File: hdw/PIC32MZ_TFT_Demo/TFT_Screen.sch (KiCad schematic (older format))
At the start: 2 parts

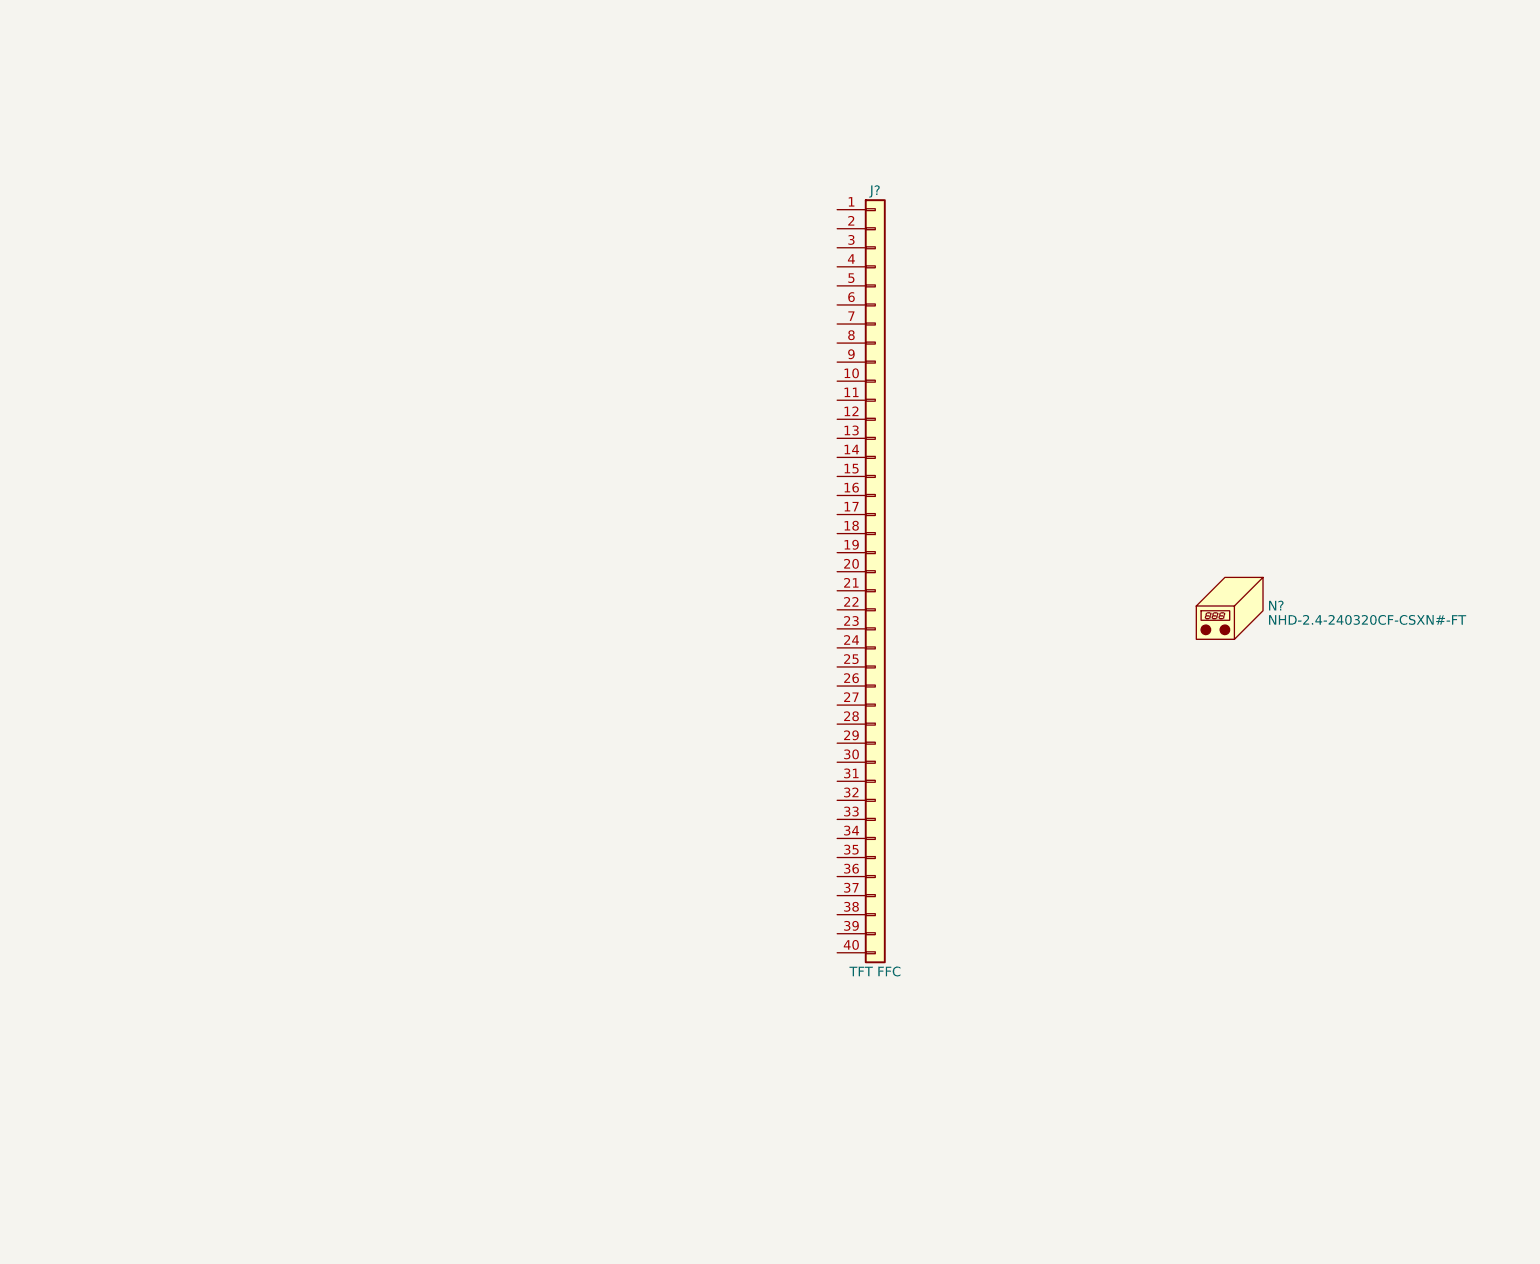
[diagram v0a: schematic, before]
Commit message: Added TFT screen sch sheet
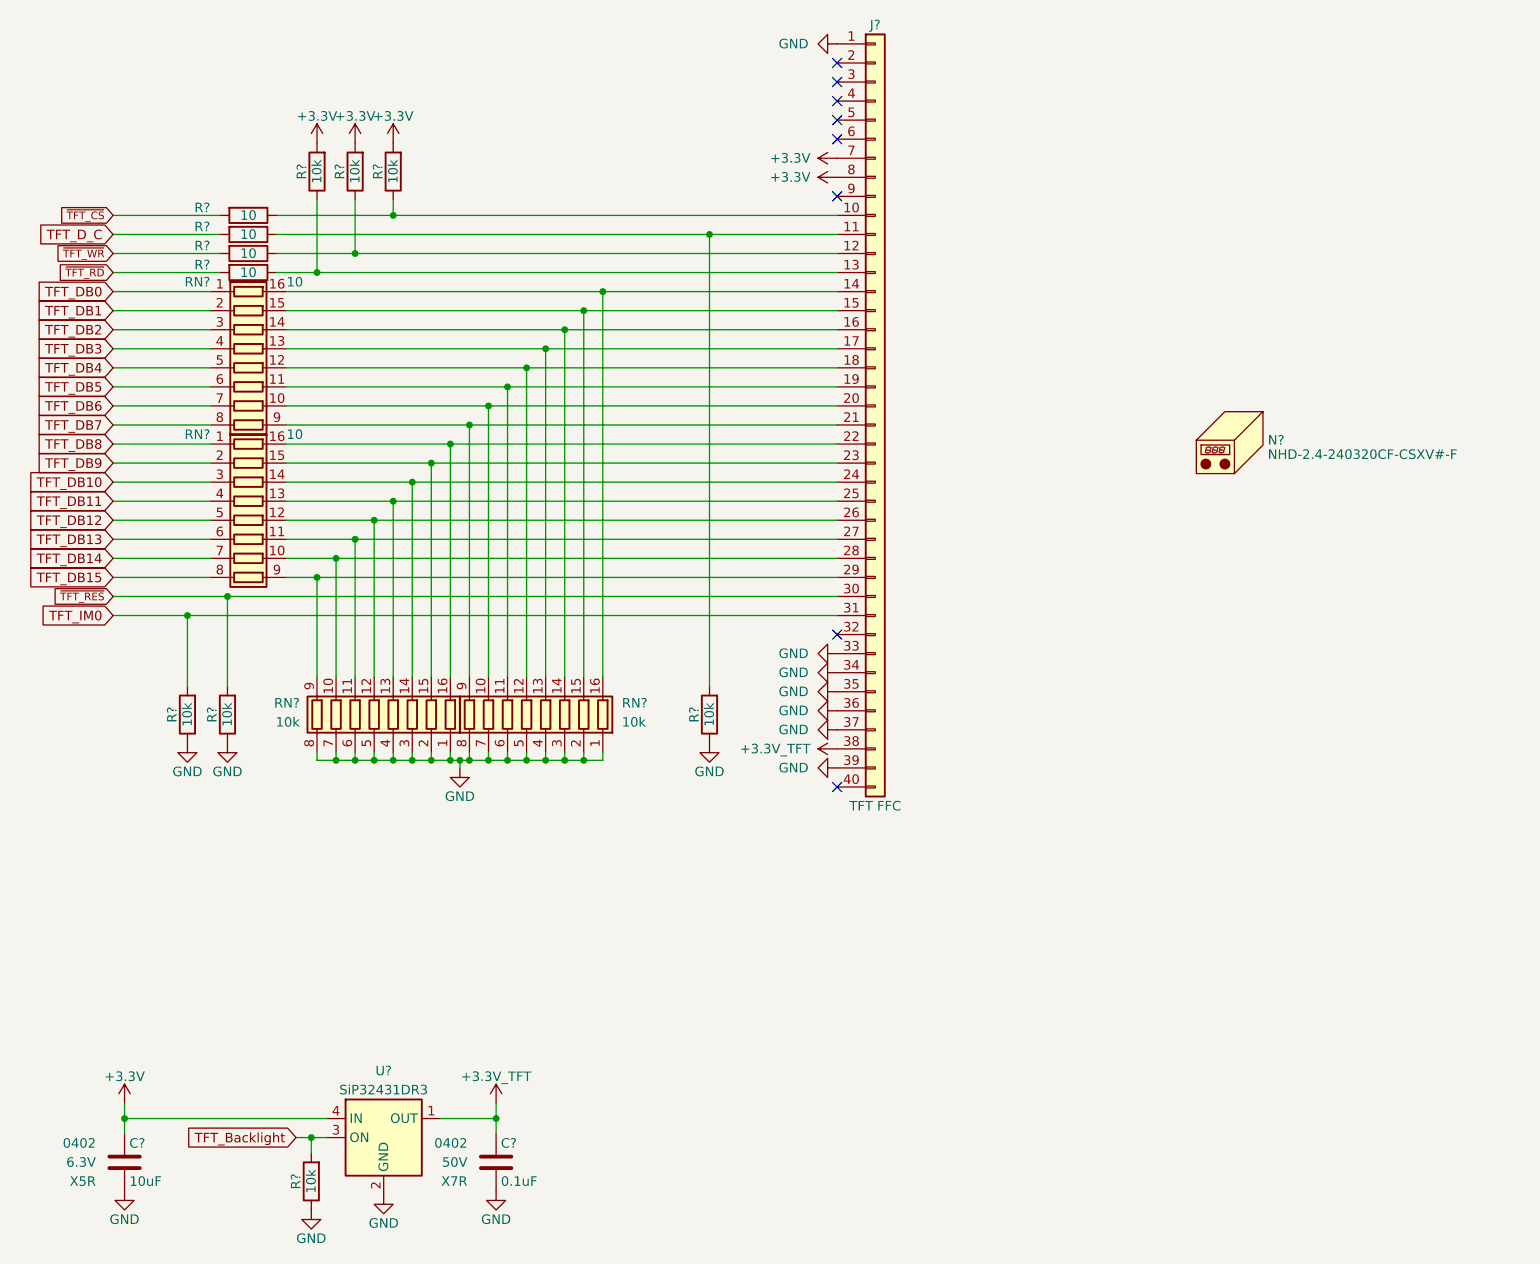
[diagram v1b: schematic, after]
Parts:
- added C?: 0.1uF, Capacitors_SMD:C_0402, symbol Custom_Library:C_Custom
- added C?: 10uF, Capacitors_SMD:C_0402, symbol Custom_Library:C_Custom
- added R? (x4): 10, Resistors_SMD:R_0402, symbol Custom_Library:R_Custom
- added R? (x7): 10k, Resistors_SMD:R_0402, symbol Custom_Library:R_Custom
- added RN? (x2): 10, symbol Device:R_Pack08
- added RN? (x2): 10k, symbol Device:R_Pack08
- added U?: SiP32431DR3, Package_TO_SOT_SMD:SOT-363_SC-70-6, symbol Power_Management:SiP32431DR3
- N?: value NHD-2.4-240320CF-CSXN#-FT -> NHD-2.4-240320CF-CSXV#-F; Digi-Key PN NHD-2.4-240320CF-CSXN#-FT-ND -> NHD-2.4-240320CF-CSXV#-F-ND
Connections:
- net GND: now reaches J?.1 (Pin_1)
- net GND: now also J?.33 (Pin_33), J?.34 (Pin_34), J?.35 (Pin_35), J?.36 (Pin_36), J?.37 (Pin_37), J?.39 (Pin_39), C?.2, C?.2, R?.2, R?.2, R?.2, R?.2, RN?.1 (R1.1), RN?.1 (R1.1), RN?.2 (R2.1), RN?.2 (R2.1), RN?.3 (R3.1), RN?.3 (R3.1), RN?.4 (R4.1), RN?.4 (R4.1), RN?.5 (R5.1), RN?.5 (R5.1), RN?.6 (R6.1), RN?.6 (R6.1), RN?.7 (R7.1), RN?.7 (R7.1), RN?.8 (R8.1), RN?.8 (R8.1), U?.2 (GND), U?.5 (GND)
- net at J?.10 (Pin_10): now also R?.2, R?.2
- net at J?.11 (Pin_11): now also R?.1, R?.2
- net at J?.12 (Pin_12): now also R?.2, R?.2
- net at J?.13 (Pin_13): now also R?.2, R?.2
- net at J?.14 (Pin_14): now also RN?.16 (R1.2), RN?.16 (R1.2)
- net at J?.15 (Pin_15): now also RN?.15 (R2.2), RN?.15 (R2.2)
- net at J?.16 (Pin_16): now also RN?.14 (R3.2), RN?.14 (R3.2)
- net at J?.17 (Pin_17): now also RN?.13 (R4.2), RN?.13 (R4.2)
- net at J?.18 (Pin_18): now also RN?.12 (R5.2), RN?.12 (R5.2)
- net at J?.19 (Pin_19): now also RN?.11 (R6.2), RN?.11 (R6.2)
- net at J?.20 (Pin_20): now also RN?.10 (R7.2), RN?.10 (R7.2)
- net at J?.21 (Pin_21): now also RN?.9 (R8.2), RN?.9 (R8.2)
- net at J?.22 (Pin_22): now also RN?.16 (R1.2), RN?.16 (R1.2)
- net at J?.23 (Pin_23): now also RN?.15 (R2.2), RN?.15 (R2.2)
- net at J?.24 (Pin_24): now also RN?.14 (R3.2), RN?.14 (R3.2)
- net at J?.25 (Pin_25): now also RN?.13 (R4.2), RN?.13 (R4.2)
- net at J?.26 (Pin_26): now also RN?.12 (R5.2), RN?.12 (R5.2)
- net at J?.27 (Pin_27): now also RN?.11 (R6.2), RN?.11 (R6.2)
- net at J?.28 (Pin_28): now also RN?.10 (R7.2), RN?.10 (R7.2)
- net at J?.29 (Pin_29): now also RN?.9 (R8.2), RN?.9 (R8.2)
- net ~TFT_RES: now reaches J?.30 (Pin_30)
- net ~TFT_RES: now also R?.1
- net TFT_IM0: now reaches J?.31 (Pin_31)
- net TFT_IM0: now also R?.1
- net +3.3V_TFT: now reaches J?.38 (Pin_38)
- net +3.3V_TFT: now also C?.1, U?.1 (OUT)
- net +3V3: now reaches J?.7 (Pin_7)
- net +3V3: now also J?.8 (Pin_8), C?.1, R?.1, R?.1, R?.1, U?.4 (IN)
- new net TFT_Backlight: R?.1, U?.3 (ON)
- new net TFT_DB0: RN?.1 (R1.1)
- new net TFT_DB1: RN?.2 (R2.1)
- new net TFT_DB10: RN?.3 (R3.1)
- new net TFT_DB11: RN?.4 (R4.1)
- new net TFT_DB12: RN?.5 (R5.1)
- new net TFT_DB13: RN?.6 (R6.1)
- new net TFT_DB14: RN?.7 (R7.1)
- new net TFT_DB15: RN?.8 (R8.1)
- new net TFT_DB2: RN?.3 (R3.1)
- new net TFT_DB3: RN?.4 (R4.1)
- new net TFT_DB4: RN?.5 (R5.1)
- new net TFT_DB5: RN?.6 (R6.1)
- new net TFT_DB6: RN?.7 (R7.1)
- new net TFT_DB7: RN?.8 (R8.1)
- new net TFT_DB8: RN?.1 (R1.1)
- new net TFT_DB9: RN?.2 (R2.1)
- new net TFT_D_C: R?.1
- new net ~TFT_CS: R?.1
- new net ~TFT_RD: R?.1
- new net ~TFT_WR: R?.1
- no-connect marks 0 -> 8
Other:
- moved on the sheet: J?, N?

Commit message: Started PCB layout
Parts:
- removed RN? (x2): 10, symbol Device:R_Pack08
- removed RN?: 10k, symbol Device:R_Pack08
- added C1102: 0.1uF, Capacitors_SMD:C_0402, symbol Custom_Library:C_Custom
- added C1104: 10nF, Capacitors_SMD:C_0402, symbol Custom_Library:C_Custom
- added C1105: 1nF, Capacitors_SMD:C_0402, symbol Custom_Library:C_Custom
- added C1106: 10uF, Capacitors_SMD:C_0402, symbol Custom_Library:C_Custom
- added RN1101, RN1102: 10, Resistors_SMD:R_Array_Convex_8x0602, symbol Device:R_Pack08
- added RN1104: 10k, Resistors_SMD:R_Array_Convex_8x0602, symbol Device:R_Pack08
- J1101: renamed from J?; footprint (none) -> Custom Footprints Library:MOLEX_0541324062; Digi-Key PN (none) -> WM3436CT-ND
- RN1103: renamed from RN?; footprint (none) -> Resistors_SMD:R_Array_Convex_8x0602; Digi-Key PN (none) -> Y1103CT-ND
- U1101: renamed from U?; Digi-Key PN (none) -> SIP32431DR3-T1GE3CT-ND
- gave numbers to parts that had none: 14
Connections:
- net +3V3: now also C1102.1, C1104.1, C1105.1, C1106.1
- net GND: now also C1102.2, C1104.2, C1105.2, C1106.2, RN1104.1 (R1.1), RN1104.2 (R2.1), RN1104.3 (R3.1), RN1104.4 (R4.1), RN1104.5 (R5.1), RN1104.6 (R6.1), RN1104.7 (R7.1), RN1104.8 (R8.1)
- net TFT_DB0: now also RN1101.1 (R1.1)
- net TFT_DB1: now also RN1101.2 (R2.1)
- net TFT_DB10: now also RN1102.3 (R3.1)
- net TFT_DB11: now also RN1102.4 (R4.1)
- net TFT_DB12: now also RN1102.5 (R5.1)
- net TFT_DB13: now also RN1102.6 (R6.1)
- net TFT_DB14: now also RN1102.7 (R7.1)
- net TFT_DB15: now also RN1102.8 (R8.1)
- net TFT_DB2: now also RN1101.3 (R3.1)
- net TFT_DB3: now also RN1101.4 (R4.1)
- net TFT_DB4: now also RN1101.5 (R5.1)
- net TFT_DB5: now also RN1101.6 (R6.1)
- net TFT_DB6: now also RN1101.7 (R7.1)
- net TFT_DB7: now also RN1101.8 (R8.1)
- net TFT_DB8: now also RN1102.1 (R1.1)
- net TFT_DB9: now also RN1102.2 (R2.1)
- net at J1101.14 (Pin_14): now also RN1101.16 (R1.2), RN1104.16 (R1.2)
- net at J1101.15 (Pin_15): now also RN1101.15 (R2.2), RN1104.15 (R2.2)
- net at J1101.16 (Pin_16): now also RN1101.14 (R3.2), RN1104.14 (R3.2)
- net at J1101.17 (Pin_17): now also RN1101.13 (R4.2), RN1104.13 (R4.2)
- net at J1101.18 (Pin_18): now also RN1101.12 (R5.2), RN1104.12 (R5.2)
- net at J1101.19 (Pin_19): now also RN1101.11 (R6.2), RN1104.11 (R6.2)
- net at J1101.20 (Pin_20): now also RN1101.10 (R7.2), RN1104.10 (R7.2)
- net at J1101.21 (Pin_21): now also RN1101.9 (R8.2), RN1104.9 (R8.2)
- net at J1101.22 (Pin_22), RN1103.16 (R1.2): now also RN1102.16 (R1.2)
- net at J1101.23 (Pin_23), RN1103.15 (R2.2): now also RN1102.15 (R2.2)
- net at J1101.24 (Pin_24), RN1103.14 (R3.2): now also RN1102.14 (R3.2)
- net at J1101.25 (Pin_25), RN1103.13 (R4.2): now also RN1102.13 (R4.2)
- net at J1101.26 (Pin_26), RN1103.12 (R5.2): now also RN1102.12 (R5.2)
- net at J1101.27 (Pin_27), RN1103.11 (R6.2): now also RN1102.11 (R6.2)
- net at J1101.28 (Pin_28), RN1103.10 (R7.2): now also RN1102.10 (R7.2)
- net at J1101.29 (Pin_29), RN1103.9 (R8.2): now also RN1102.9 (R8.2)
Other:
- moved on the sheet: J1101, N1101, R1101, R1102, R1103, R1104, R1105, R1106, R1108, R1109, R1110, R1111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
